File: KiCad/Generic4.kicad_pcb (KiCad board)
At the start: 2 copper layers, 13.2 x 19.5 mm, 15 parts, among them J1 I/O, J2 SPOX, U1 ESP32-PICO-MINI-02, U2 LMR16006+FB

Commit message: Tweak
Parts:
- moved D2 1.63 mm to (97.6, 44.8)
- moved C1 1.63 mm to (102.0, 41.9)
- moved C2 1.63 mm to (100.7, 45.1)
- moved C3 1.63 mm to (94.5, 45.1)
- moved L1 1.63 mm to (96.0, 41.6)
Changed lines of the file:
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@@
   )
   (footprint "RevK:Hidden" (layer "B.Cu")
-    (at 96 45.65 -90)
+    (at 94.45 45.15 -90)
     (property "Note" "0603 or 0805")
     (property "Part No" "")
@@
   )
   (footprint "RevK:Hidden" (layer "B.Cu")
-    (at 99.12 45.27)
+    (at 97.57 44.77)
     (property "Manufacturer" "Bourns")
     (property "Note" "")
@@
   )
   (footprint "RevK:Hidden" (layer "B.Cu")
-    (at 103.5 42.35 -90)
+    (at 101.95 41.85 -90)
     (property "Note" "X7R or X5R 0603")
     (property "Part No" "")
@@
   )
   (footprint "RevK:Hidden" (layer "B.Cu")
-    (at 102.25 45.65 -90)
+    (at 100.7 45.15 -90)
     (property "Note" "0603 or 0805")
     (property "Part No" "")
@@
   )
   (footprint "RevK:Hidden" (layer "B.Cu")
-    (at 97.5 42.1)
+    (at 95.95 41.6)
     (property "Manufacturer" "Laird")
     (property "Note" "")

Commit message: Tidy
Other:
- board text added: "RGB: 22/19/7"
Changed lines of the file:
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@@
     (effects (font (size 1 1) (thickness 0.15)) (justify mirror))
+  )
+  (gr_text "RGB: 22/19/7" (at 97.7 47.2) (layer "B.SilkS")
+    (effects (font (size 0.75 0.75) (thickness 0.1)) (justify mirror))
   )
   (gr_text "25" (at 94.02 55.69 45) (layer "B.SilkS")

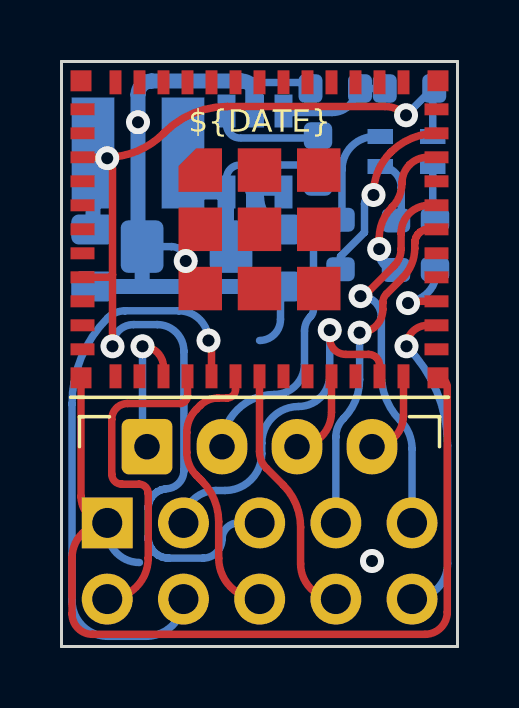
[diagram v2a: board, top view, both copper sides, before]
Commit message: Tweak for smoother power, and change of regulator FB pot divide
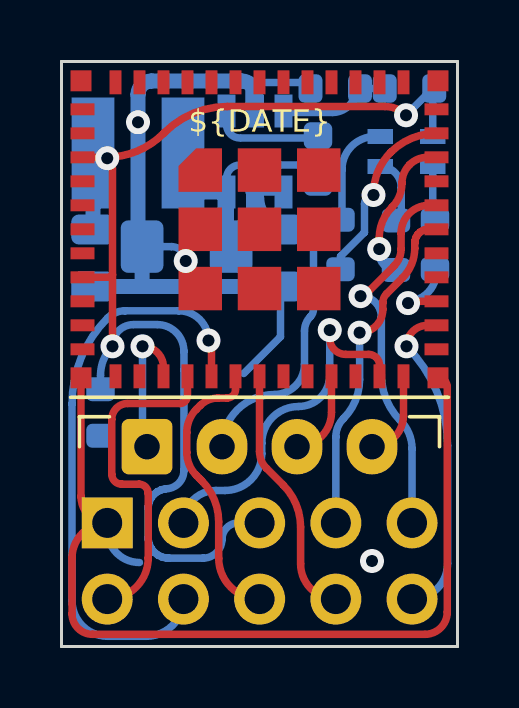
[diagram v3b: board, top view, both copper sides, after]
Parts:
- added C4: 10nF, RevK:C_0603, B.Cu at (94.7, 50.3)
- R4: value 10M 1% or 0R -> 100k 1% or 0R
- R5: value 3M 1% or NF -> 30k 1% or NF
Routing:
- net EN: track 36.6 -> 38.1 mm
- net GND: track 43.8 -> 45.1 mm
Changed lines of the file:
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@@
     )
   )
-  (property "DATE" "2022-03-10")
+  (property "DATE" "2022-03-16")
   (net 0 "")
   (net 1 "GND")
@@
       (effects (font (size 0.5 0.5) (thickness 0.08)) (justify mirror))
     )
-    (fp_text value "3M 1% or NF" (at 0 0) (layer "B.Fab")
+    (fp_text value "30k 1% or NF" (at 0 0) (layer "B.Fab")
       (effects (font (size 0.4 0.4) (thickness 0.08)) (justify mirror))
     )
@@
     (model "${KICAD6_3DMODEL_DIR}/LED_SMD.3dshapes/LED_0603_1608Metric.wrl"
       (offset (xyz 0 0.4 0))
+      (scale (xyz 1 1 1))
+      (rotate (xyz 0 0 0))
+    )
+  )
+  (footprint "RevK:C_0603" (layer "B.Cu")
+    (at 94.7 50.3 -90)
+    (descr "Capacitor SMD 0603 (1608 Metric), square (rectangular) end terminal, IPC_7351 nominal, (Body size source: IPC-SM-782 page 76, https://www.pcb-3d.com/wordpress/wp-content/uploads/ipc-sm-782a_amendment_1_and_2.pdf), generated with kicad-footprint-generator")
+    (tags "capacitor")
+    (property "Sheetfile" "Generic4.kicad_sch")
+    (property "Sheetname" "")
+    (attr smd)
+    (fp_text reference "C4" (at -1.6 0) (layer "B.SilkS") hide
+      (effects (font (size 0.5 0.5) (thickness 0.08)) (justify mirror))
+    )
+    (fp_text value "10nF" (at 0 0 90) (layer "B.Fab")
+      (effects (font (size 0.4 0.4) (thickness 0.08)) (justify mirror))
+    )
+    (fp_text user "${REFERENCE}" (at 0 0.8 90) (layer "B.Fab")
+      (effects (font (size 0.4 0.4) (thickness 0.06)) (justify mirror))
+    )
+    (fp_line (start -0.3 0.5) (end 0.3 0.5) (layer "B.SilkS") (width 0.12))
+    (fp_line (start -0.3 -0.5) (end 0.3 -0.5) (layer "B.SilkS") (width 0.12))
+    (fp_line (start 0.8 0.4) (end 0.8 -0.4) (layer "B.CrtYd") (width 0.05))
+    (fp_line (start 0.8 -0.4) (end -0.8 -0.4) (layer "B.CrtYd") (width 0.05))
+    (fp_line (start -0.8 -0.4) (end -0.8 0.4) (layer "B.CrtYd") (width 0.05))
+    (fp_line (start -0.8 0.4) (end 0.8 0.4) (layer "B.CrtYd") (width 0.05))
+    (fp_line (start -0.8 0.4) (end 0.8 0.4) (layer "B.Fab") (width 0.1))
+    (fp_line (start 0.8 -0.4) (end -0.8 -0.4) (layer "B.Fab") (width 0.1))
+    (fp_line (start -0.8 -0.4) (end -0.8 0.4) (layer "B.Fab") (width 0.1))
+    (fp_line (start 0.8 0.4) (end 0.8 -0.4) (layer "B.Fab") (width 0.1))
+    (pad "1" smd roundrect (at -0.775 0 270) (size 0.8 0.95) (layers "B.Cu" "B.Paste" "B.Mask") (roundrect_rratio 0.25)
+      (net 11 "EN") (pintype "passive"))
+    (pad "2" smd roundrect (at 0.775 0 270) (size 0.8 0.95) (layers "B.Cu" "B.Paste" "B.Mask") (roundrect_rratio 0.25)
+      (net 1 "GND") (pintype "passive"))
+    (model "${KICAD6_3DMODEL_DIR}/Capacitor_SMD.3dshapes/C_0603_1608Metric.step"
+      (offset (xyz 0 0 0))
       (scale (xyz 1 1 1))
       (rotate (xyz 0 0 0))
@@
       (effects (font (size 0.5 0.5) (thickness 0.08)) (justify mirror))
     )
-    (fp_text value "10M 1% or 0R" (at 0 0) (layer "B.Fab")
+    (fp_text value "100k 1% or 0R" (at 0 0) (layer "B.Fab")
       (effects (font (size 0.4 0.4) (thickness 0.08)) (justify mirror))
     )
@@
     (effects (font (size 0.5 0.5) (thickness 0.1)) (justify mirror))
   )
-  (gr_text "⏚" (at 94.5 51.5) (layer "B.SilkS")
+  (gr_text "⏚" (at 94.6 52.3) (layer "B.SilkS")
     (effects (font (size 1 1) (thickness 0.15)) (justify mirror))
   )
@@
   (arc (start 93.750489 55.154511) (mid 94.094495 54.324006) (end 94.925 53.98) (width 0.25) (layer "F.Cu") (net 1))
   (arc (start 94.05 53.105) (mid 94.306282 53.723718) (end 94.925 53.98) (width 0.25) (layer "F.Cu") (net 1))
+  (segment (start 100.7 47.775) (end 100.7 46.1) (width 0.25) (layer "B.Cu") (net 1))
   (segment (start 99.65 39.45) (end 99.65 40.25) (width 0.25) (layer "B.Cu") (net 1))
   (segment (start 94.925 53.98) (end 94.925 54.225) (width 0.25) (layer "B.Cu") (net 1))
-  (segment (start 100.7 46.1) (end 100.7 47.2) (width 0.25) (layer "B.Cu") (net 1))
   (segment (start 101.575 39.5) (end 101.375 39.3) (width 0.25) (layer "B.Cu") (net 1))
+  (segment (start 99.475 49) (end 100.7 47.775) (width 0.25) (layer "B.Cu") (net 1))
   (segment (start 96.1 48.093748) (end 96.1 51.29) (width 0.25) (layer "B.Cu") (net 1))
   (segment (start 101.375 39.3) (end 99.8 39.3) (width 0.25) (layer "B.Cu") (net 1))
   (segment (start 95.8875 44.77) (end 97.0605 44.77) (width 0.25) (layer "B.Cu") (net 1))
-  (arc (start 100.7 47.2) (mid 100.494975 47.694975) (end 100 47.9) (width 0.25) (layer "B.Cu") (net 1))
   (arc (start 96.1 51.29) (mid 96.143934 51.396066) (end 96.25 51.44) (width 0.25) (layer "B.Cu") (net 1))
   (arc (start 97.0605 44.77) (mid 97.399911 44.910589) (end 97.5405 45.25) (width 0.25) (layer "B.Cu") (net 1))
@@
   (segment (start 95.099502 48.069646) (end 95.099502 48.093748) (width 0.25) (layer "B.Cu") (net 11))
   (segment (start 96.290489 53.493501) (end 96.292145 53.42028) (width 0.25) (layer "B.Cu") (net 11))
+  (segment (start 94.7 49.058231) (end 94.7 49.525) (width 0.25) (layer "B.Cu") (net 11))
   (segment (start 96.388269 53.145572) (end 96.479574 53.03108) (width 0.25) (layer "B.Cu") (net 11))
   (segment (start 105.775 39.55) (end 105.825 39.5) (width 0.25) (layer "B.Cu") (net 11))
@@
   (segment (start 96.726005 52.876237) (end 96.868774 52.843651) (width 0.25) (layer "B.Cu") (net 11))
   (segment (start 96.611088 55.051233) (end 96.490184 54.954816) (width 0.25) (layer "B.Cu") (net 11))
-  (segment (start 97.480569 52.231856) (end 97.480569 48.255969) (width 0.25) (layer "B.Cu") (net 11))
   (segment (start 96.292145 53.42028) (end 96.324731 53.277511) (width 0.25) (layer "B.Cu") (net 11))
   (segment (start 96.750416 55.11833) (end 96.611088 55.051233) (width 0.25) (layer "B.Cu") (net 11))
@@
   (segment (start 96.324731 53.277511) (end 96.388269 53.145572) (width 0.25) (layer "B.Cu") (net 11))
   (segment (start 96.978501 55.154511) (end 96.90118 55.152741) (width 0.25) (layer "B.Cu") (net 11))
+  (segment (start 97.480569 48.880569) (end 97.480569 48.255969) (width 0.25) (layer "B.Cu") (net 11))
   (segment (start 96.593847 47.369247) (end 95.799901 47.369247) (width 0.25) (layer "B.Cu") (net 11))
+  (segment (start 97.480569 52.231856) (end 97.480569 48.880569) (width 0.25) (layer "B.Cu") (net 11))
   (arc (start 105.740619 39.534952) (mid 105.779333 39.509084) (end 105.825 39.5) (width 0.25) (layer "B.Cu") (net 11))
   (arc (start 96.868774 52.843651) (mid 97.301378 52.66446) (end 97.480569 52.231856) (width 0.25) (layer "B.Cu") (net 11))
+  (arc (start 95.099502 48.093748) (mid 94.803827 48.536256) (end 94.7 49.058231) (width 0.25) (layer "B.Cu") (net 11))
   (arc (start 99.295 53.98) (mid 98.909627 54.139627) (end 98.75 54.525) (width 0.25) (layer "B.Cu") (net 11))
   (arc (start 97.480569 48.255969) (mid 97.220854 47.628962) (end 96.593847 47.369247) (width 0.25) (layer "B.Cu") (net 11))

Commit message: Change resistor values
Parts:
- C4: value 10nF -> 100nF
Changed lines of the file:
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@@
       (effects (font (size 0.5 0.5) (thickness 0.08)) (justify mirror))
     )
-    (fp_text value "10nF" (at 0 0 90) (layer "B.Fab")
+    (fp_text value "100nF" (at 0 0 90) (layer "B.Fab")
       (effects (font (size 0.4 0.4) (thickness 0.08)) (justify mirror))
     )

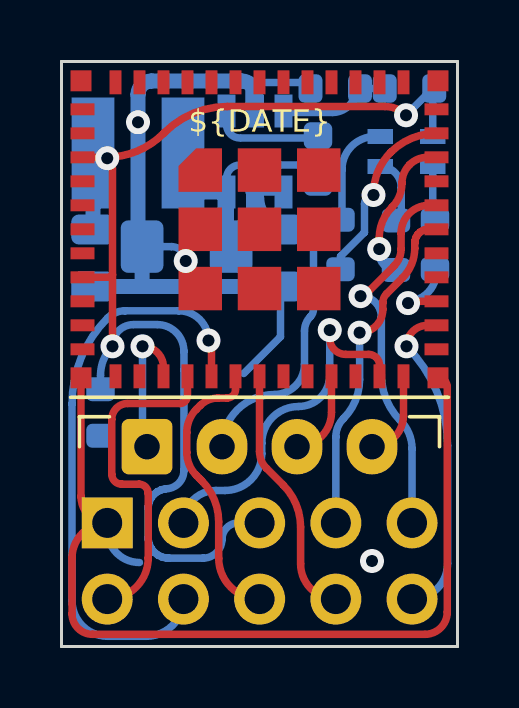
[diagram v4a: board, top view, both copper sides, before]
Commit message: Changed to have C/R for EN
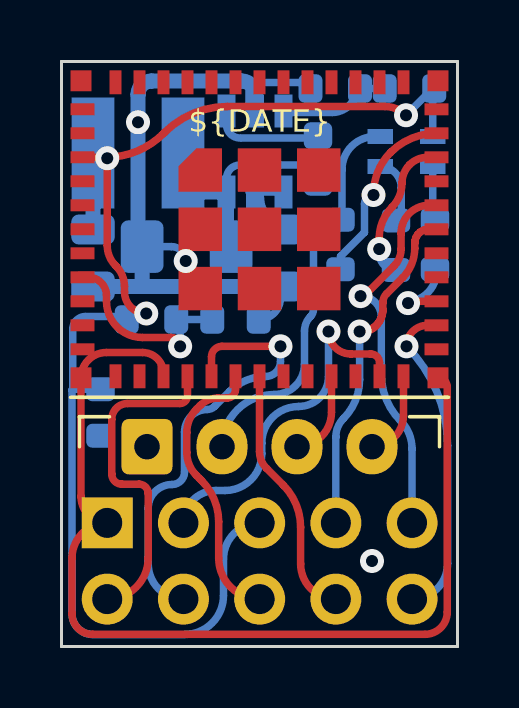
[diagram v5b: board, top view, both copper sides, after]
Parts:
- added C1: 10nF, RevK:C_0603, B.Cu at (99.2, 47.2)
- added R4: 10K, RevK:R_0603, B.Cu at (96.4, 47.2)
- renumbered C1 to C3, C2 to C4, C3 to C5, C4 to C6, R4 to R5, R5 to R6
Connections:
- C6 pad 1: EN -> +3V3
- D1 pad 1: EN -> +3V3
- J1 pad 5: EN -> +3V3
- R5 pad 1: EN -> +3V3
- U1 pad 3: EN -> +3V3
- U2 pad 4: EN -> +3V3
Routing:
- net +3V3: track 0.00 -> 42.5 mm, vias 0 -> 3
- net EN: track 38.1 -> 6.50 mm, vias 3 -> 1
- net IO2: track 19.9 -> 14.7 mm
- net GND: track 45.1 -> 40.1 mm, vias 4 -> 3
- net RX: track 11.3 -> 12.4 mm
